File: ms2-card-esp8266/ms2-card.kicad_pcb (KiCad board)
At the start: 2 copper layers, 100 x 54 mm, 62 parts, among them J1 Schaltregler, J10 MicroSD_SPI_CD, J11 Conn_01x06, J2 ESP Prog, J20 Smartcard Connector, J21 PogoPin, J22 Card Edge, J23 Conn_01x04, J30 USB_B_Micro, J31 Power Select, J32 Conn_01x03, Q1 MMBT3904, Q2 MMBT3904, Q3 MMBT5401, SW1 RESET, U1 ESP-12F, U2 FM24C64B, U20 BL1551B, U3 BL1551B, U30 CP2102N-Axx-xQFN24, U4 BL1551B, U6 AMS1117-3.3

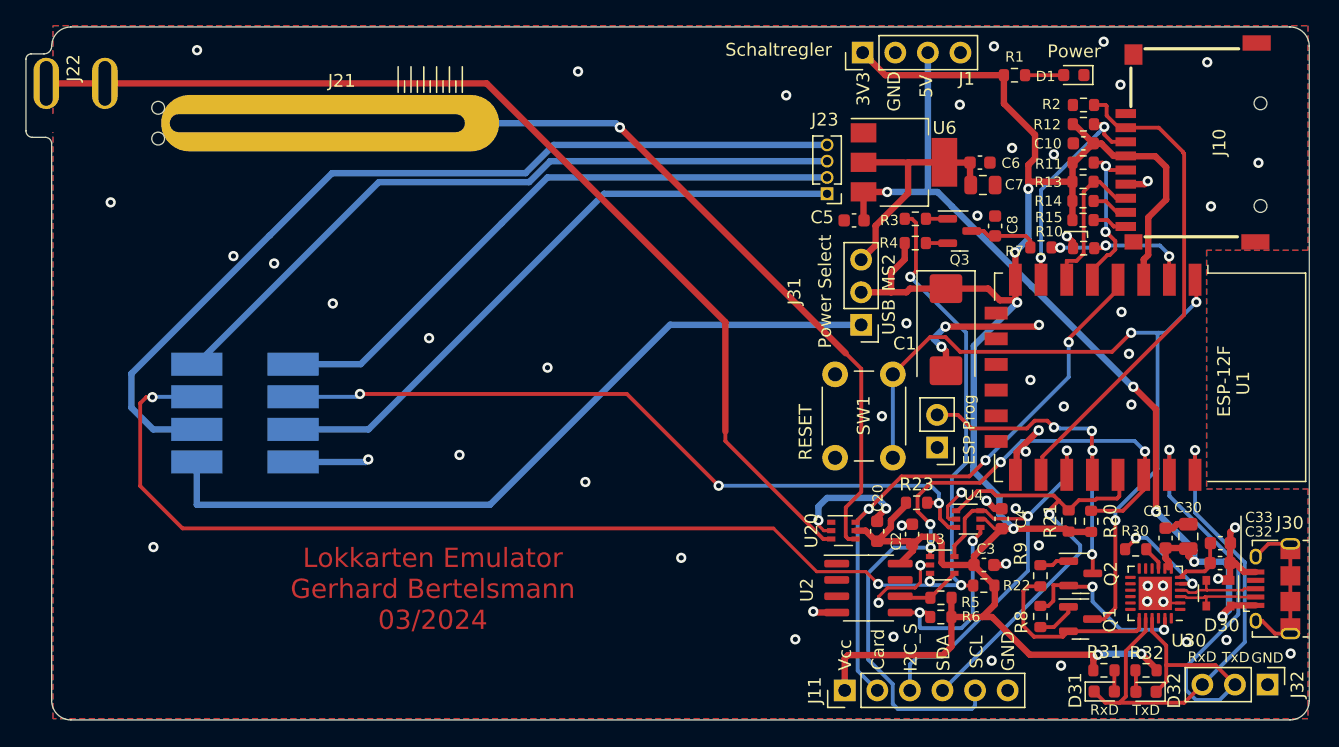
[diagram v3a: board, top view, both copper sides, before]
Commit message: use wider wires for card connnects
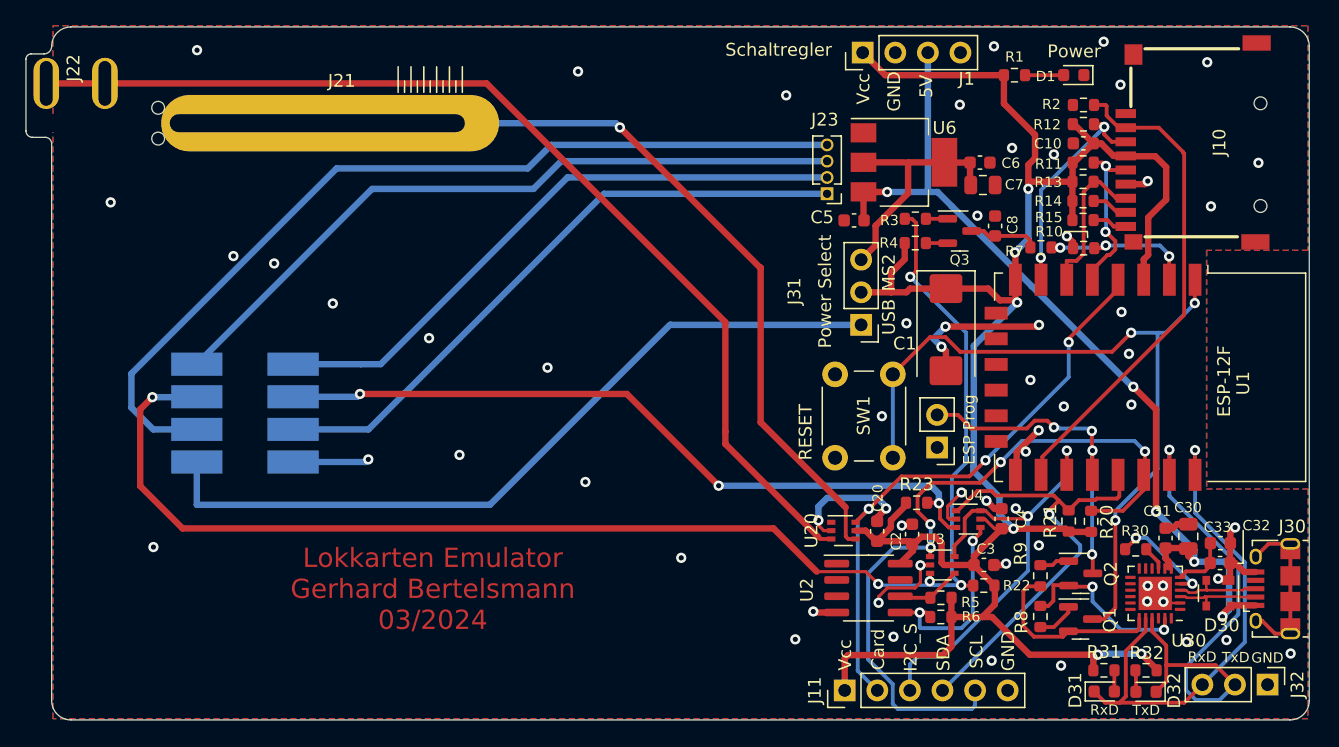
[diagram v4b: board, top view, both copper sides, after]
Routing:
- net Net-(J20-Pad2): track 91.5 -> 70.0 mm
- net Net-(J20-Pad5): track 69.6 -> 68.0 mm
- net /PP: track 64.7 -> 63.8 mm
- net Net-(J22-Pad1): track 81.3 -> 82.2 mm
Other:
- board text removed: "3V3"

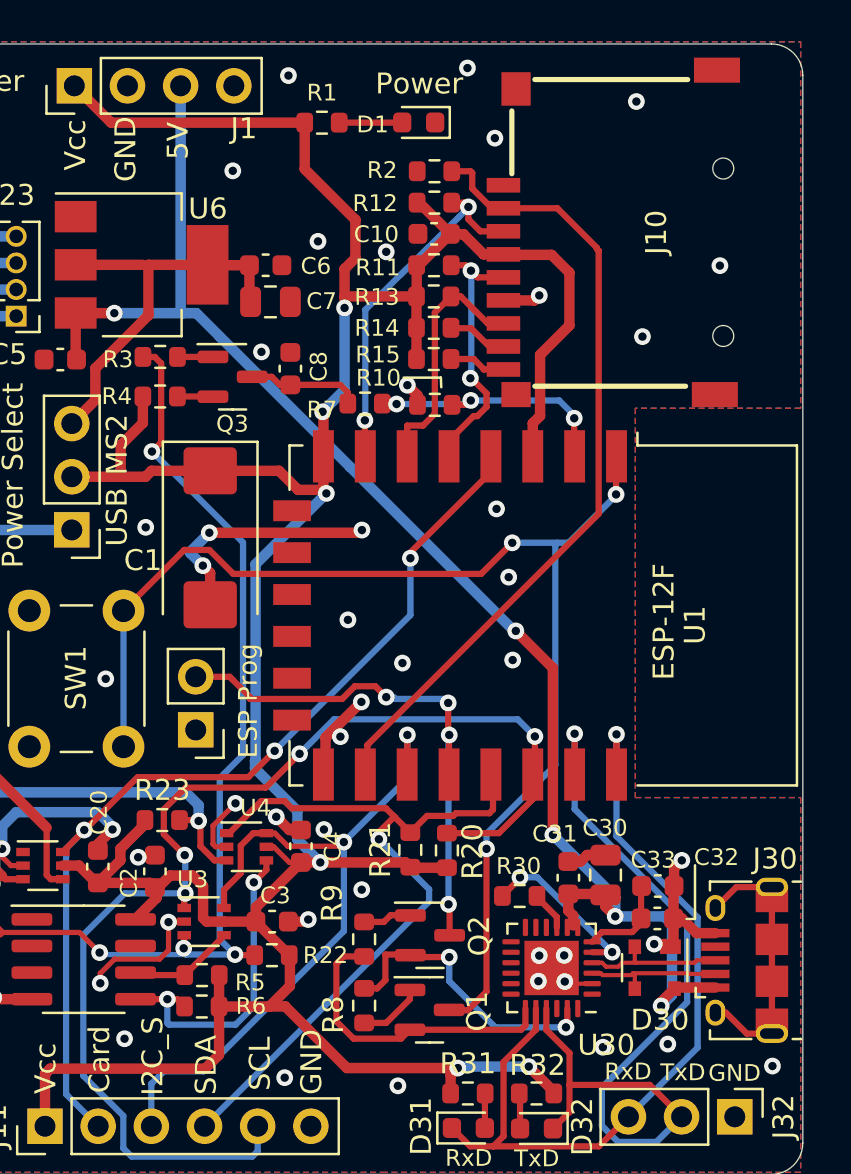
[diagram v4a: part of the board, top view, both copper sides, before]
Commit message: move JLC order number behind SD card
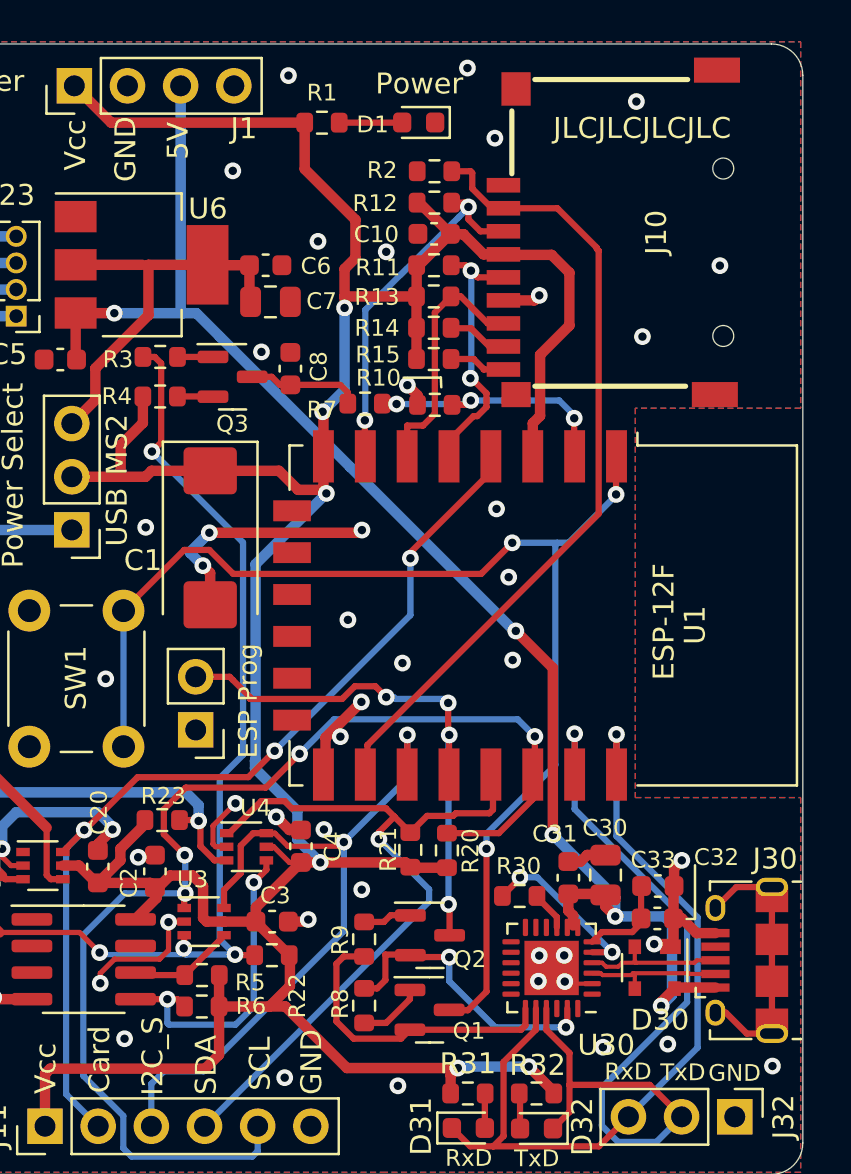
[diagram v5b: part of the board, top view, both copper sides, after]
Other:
- board text added: "JLCJLCJLCJLC"
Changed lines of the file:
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@@
+      (rotate (xyz 0 0 0))
+    )
+    (model "${KICAD6_3DMODEL_DIR}/Capacitor_SMD.3dshapes/CP_Elec_6.3x5.4.wrl" hide
+      (offset (xyz 0 0 0))
+      (scale (xyz 1 1 1))
       (rotate (xyz 0 0 0))
     )
@@
     (property "Sheetname" "")
     (attr smd)
-    (fp_text reference "R20" (at -0.05 1.225 90) (layer "F.SilkS")
-      (effects (font (size 1 1) (thickness 0.15)))
+    (fp_text reference "R20" (at -0.025 1.125 90) (layer "F.SilkS")
+      (effects (font (size 0.8 0.8) (thickness 0.15)))
     )
     (fp_text value "4k7" (at 0 1.43 90) (layer "F.Fab") hide
@@
     (property "Sheetname" "")
     (attr smd)
-    (fp_text reference "R23" (at 0 -1.43) (layer "F.SilkS")
-      (effects (font (size 1 1) (thickness 0.15)))
+    (fp_text reference "R23" (at 0.05 -1.15) (layer "F.SilkS")
+      (effects (font (size 0.8 0.8) (thickness 0.15)))
     )
     (fp_text value "4k7" (at 0 1.43) (layer "F.Fab") hide
@@
     (property "Sheetname" "")
     (attr smd)
-    (fp_text reference "R9" (at 1.725 -1.535 90) (layer "F.SilkS")
-      (effects (font (size 1 1) (thickness 0.15)))
+    (fp_text reference "R9" (at -0.035 -1.145 90) (layer "F.SilkS")
+      (effects (font (size 0.8 0.8) (thickness 0.15)))
     )
     (fp_text value "10k" (at 0 1.43 90) (layer "F.Fab") hide
@@
     (property "Sheetname" "")
     (attr smd)
-    (fp_text reference "R21" (at 0 -1.43 90) (layer "F.SilkS")
-      (effects (font (size 1 1) (thickness 0.15)))
+    (fp_text reference "R21" (at 0.025 -1.05 90) (layer "F.SilkS")
+      (effects (font (size 0.8 0.8) (thickness 0.15)))
     )
     (fp_text value "4k7" (at 0 1.43 90) (layer "F.Fab") hide
@@
     (property "Sheetname" "")
     (attr smd)
-    (fp_text reference "Q1" (at 2.28 0.07 90) (layer "F.SilkS")
-      (effects (font (size 1 1) (thickness 0.15)))
+    (fp_text reference "Q1" (at 1.88 1.01 180) (layer "F.SilkS")
+      (effects (font (size 0.8 0.8) (thickness 0.15)))
     )
     (fp_text value "MMBT3904" (at 0 2.4) (layer "F.Fab") hide
@@
     (property "Sheetname" "")
     (attr smd)
-    (fp_text reference "Q2" (at 2.35 0.03 90) (layer "F.SilkS")
-      (effects (font (size 1 1) (thickness 0.15)))
+    (fp_text reference "Q2" (at 1.91 1.145 180) (layer "F.SilkS")
+      (effects (font (size 0.8 0.8) (thickness 0.15)))
     )
     (fp_text value "MMBT3904" (at 0 2.4) (layer "F.Fab") hide
@@
     (property "Sheetname" "")
     (attr smd)
-    (fp_text reference "R8" (at 0.435 1.475 90) (layer "F.SilkS")
-      (effects (font (size 1 1) (thickness 0.15)))
+    (fp_text reference "R8" (at -0.09 1.145 90) (layer "F.SilkS")
+      (effects (font (size 0.8 0.8) (thickness 0.15)))
     )
     (fp_text value "10k" (at 0 1.43 90) (layer "F.Fab") hide
@@
     (property "Sheetname" "")
     (attr smd)
-    (fp_text reference "R22" (at -2.56 0) (layer "F.SilkS")
+    (fp_text reference "R22" (at -1.21 -1.945 90) (layer "F.SilkS")
       (effects (font (size 0.8 0.8) (thickness 0.15)))
     )
@@
     (effects (font (size 1 1) (thickness 0.15)))
   )
+  (gr_text "JLCJLCJLCJLC" (at 190.325 104.025) (layer "F.SilkS")
+    (effects (font (size 1 1) (thickness 0.15)))
+  )

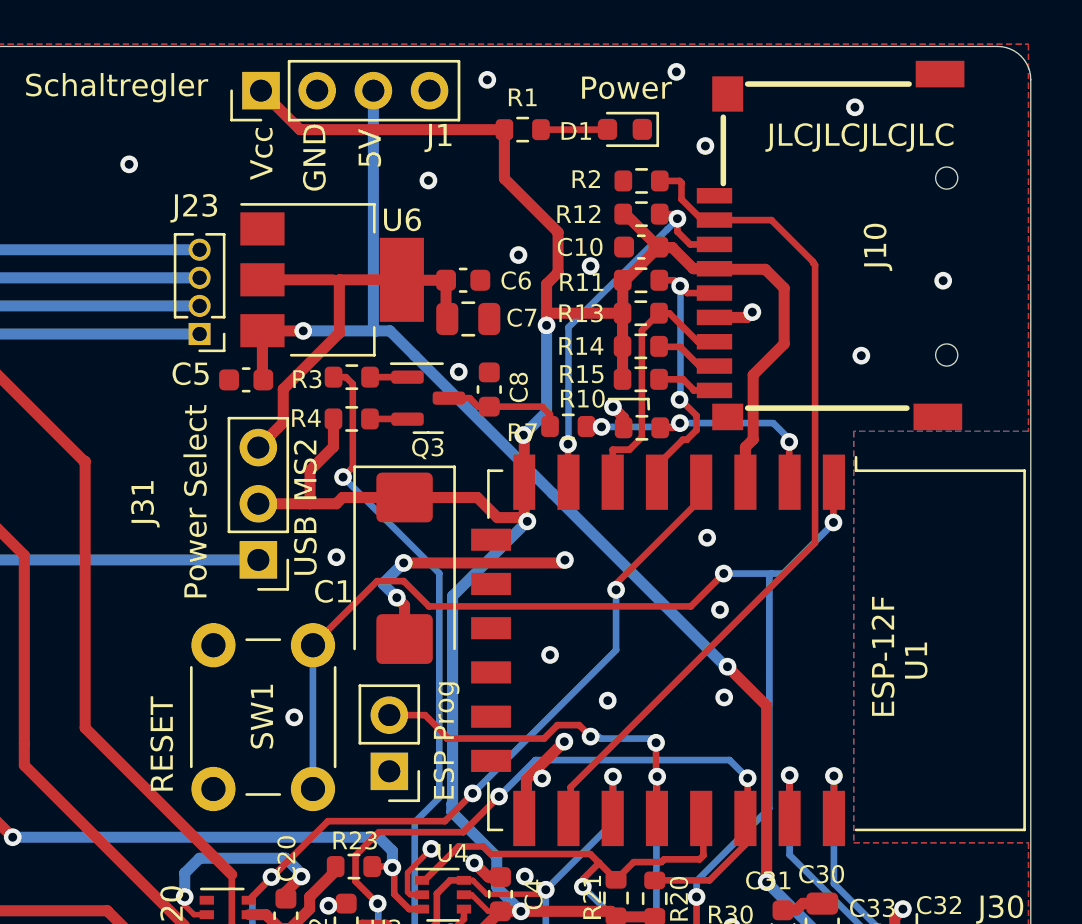
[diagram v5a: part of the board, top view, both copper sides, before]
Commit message: add SPI EEPROM alternative
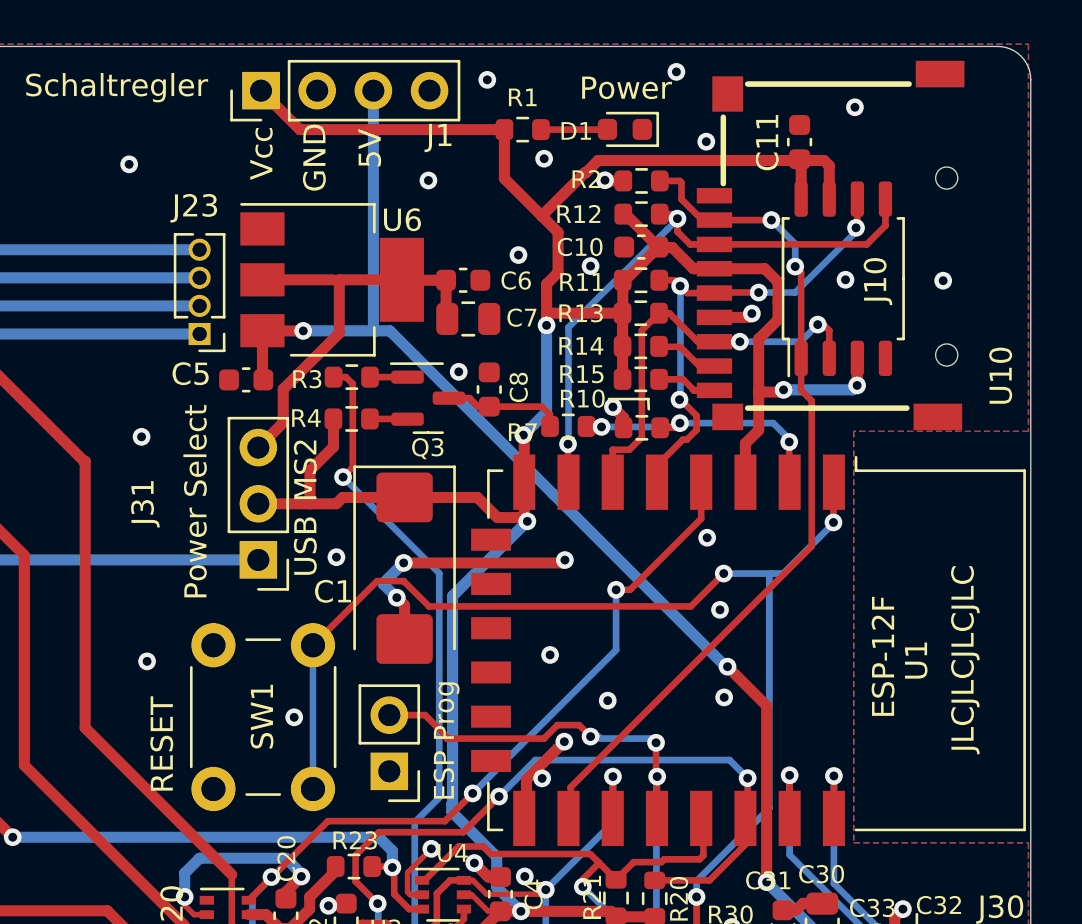
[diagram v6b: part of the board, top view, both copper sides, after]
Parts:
- added C11: 100nF, Capacitor_SMD:C_0603_1608Metric, F.Cu at (187.6, 104.3)
- added U10: W25Q128JVIM, Package_SO:SOIC-8_5.23x5.23mm_P1.27mm, F.Cu at (189.5, 110.5)
- R22, R23, R5, R6: value 4k7 -> 47k
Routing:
- net VCC: track 166.2 -> 189.3 mm, vias 6 -> 8
- net /MOSI: track 17.4 -> 26.7 mm
- net /CLK: track 12.8 -> 21.8 mm, vias 2 -> 4
- net /MISO: track 12.0 -> 18.9 mm, vias 0 -> 2
- net GND: track 60.1 -> 60.9 mm, vias 62 -> 66
- net /CS: track 38.1 -> 37.9 mm, vias 0 -> 2
